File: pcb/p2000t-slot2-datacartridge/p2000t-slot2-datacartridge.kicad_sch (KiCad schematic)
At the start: 27 parts, among them J1 P2000T Port 2, U1 74HC02, U10 ZIF, U11 CY62256-70PC, U2 74HC04, U3 74HC138, U4 74HC21, U5 74HC273, U6 74HC273, U7 74HC173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

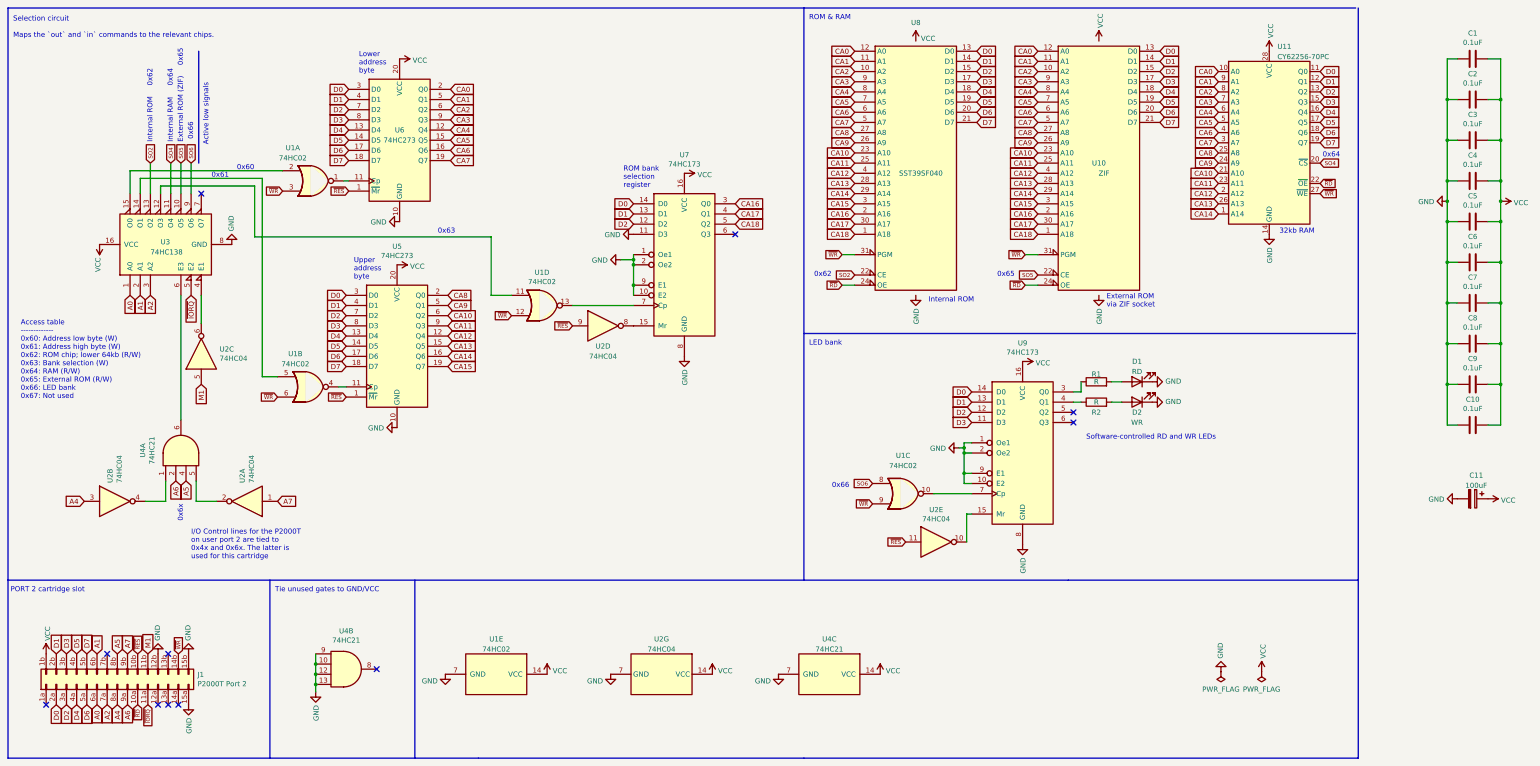
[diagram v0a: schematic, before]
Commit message: Revision 3 and 4 of the PCB (#12)
* Initial commit revision

* Interim commit

* Rerouting

* Fixing bug in PCB
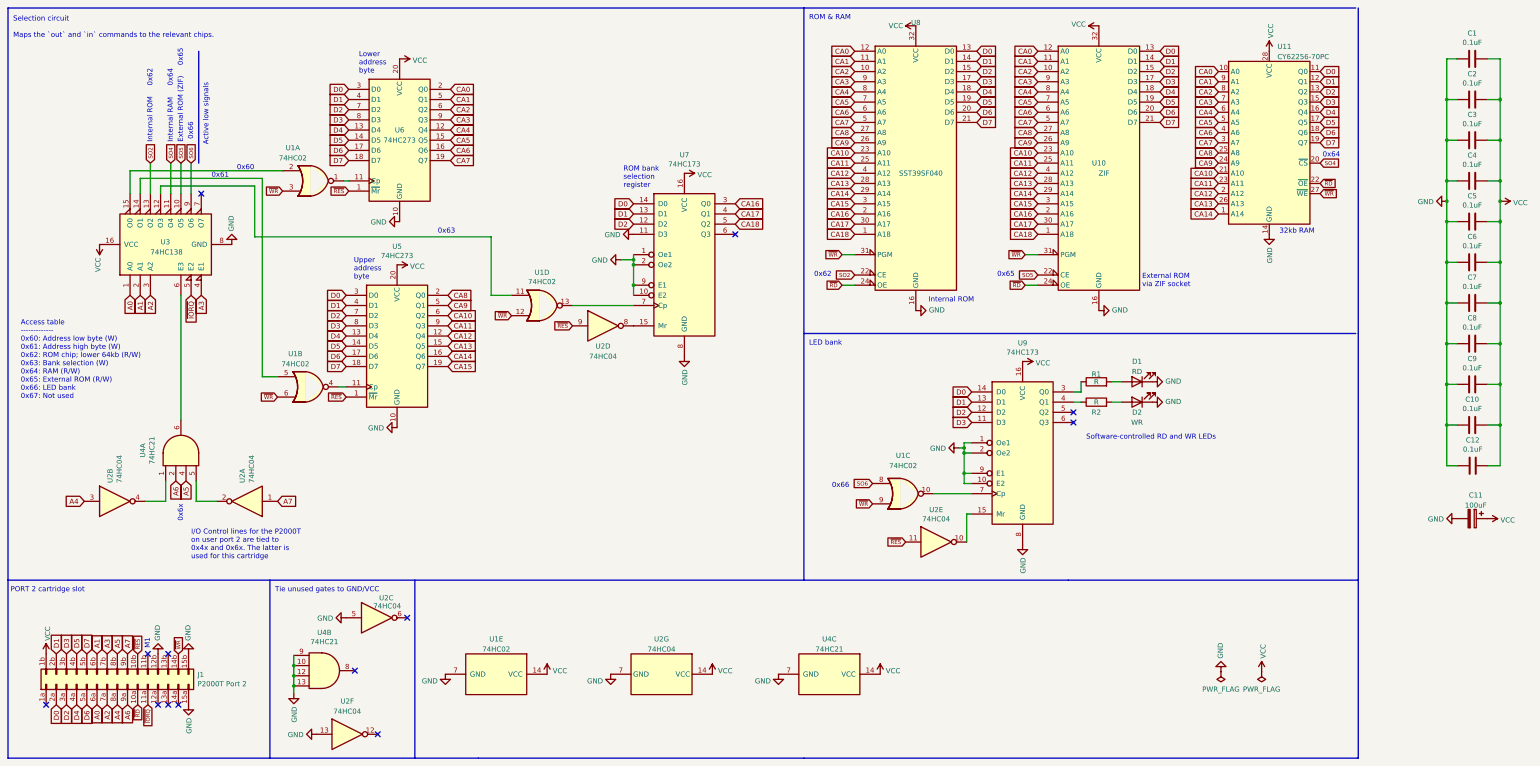
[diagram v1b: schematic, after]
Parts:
- added C12: 0.1uF, Capacitor_THT:C_Disc_D5.0mm_W2.5mm_P5.00mm, symbol Device:C
- added unit 6 of U2
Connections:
- net GND: now also U2.5, C12.2, U2.13
- net VCC: now also C12.1
- net A3: now reaches J1.7b (Pin_7b)
- net A3: now also U3.4 (E1)
- net at U2.6: no longer U3.4 (E1)
- net M1: no longer names the net of J1.11b (Pin_11b)
- net M1: no longer U2.5
- no-connect marks 11 -> 13
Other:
- note added: "M1"
- moved on the sheet: C11, U2C, U4B
